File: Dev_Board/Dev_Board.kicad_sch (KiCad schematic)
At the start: 24 parts, among them J1 Conn_01x04, J2 Conn_01x04

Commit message: 02/09/2024 sch
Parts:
- added D2, D3, D4, D5, D6, D7, D8: D, Diode_SMD:Nexperia_DSN0603-2_0.6x0.3mm_P0.4mm, symbol Device:D
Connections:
- net B2: now also D2.2 (A)
- net B3: now also D3.2 (A)
- net B4: now also D4.2 (A)
- net B5: now also D5.2 (A)
- net B6: now also D6.2 (A)
- net B7: now also D7.2 (A)
- net GND: now also In_Port1.1 (Pin_1), In_Port2.1 (Pin_1), Out_Port1.1 (Pin_1), Out_Port2.1 (Pin_1), Out_Port3.1 (Pin_1), Out_Port4.1 (Pin_1), Out_Port5.1 (Pin_1), Out_Port6.1 (Pin_1), TP4.1, TP5.1
- net +24V: now reaches Out_Port1.2 (Pin_2), Out_Port4.2 (Pin_2)
- net +24V: now also In_Port1.2 (Pin_2), In_Port2.2 (Pin_2), Out_Port2.2 (Pin_2), Out_Port3.2 (Pin_2), Out_Port5.2 (Pin_2), Out_Port6.2 (Pin_2), TP4.2, TP5.2
- net 3.3V renamed +3.3V
- net A1 renamed A1 (GND)
- net A8 renamed A8M (GND)
- net B1 renamed B1 (5V)
- net B8 renamed B8 (5V)
- net B8 (5V): now also D8.2 (A)

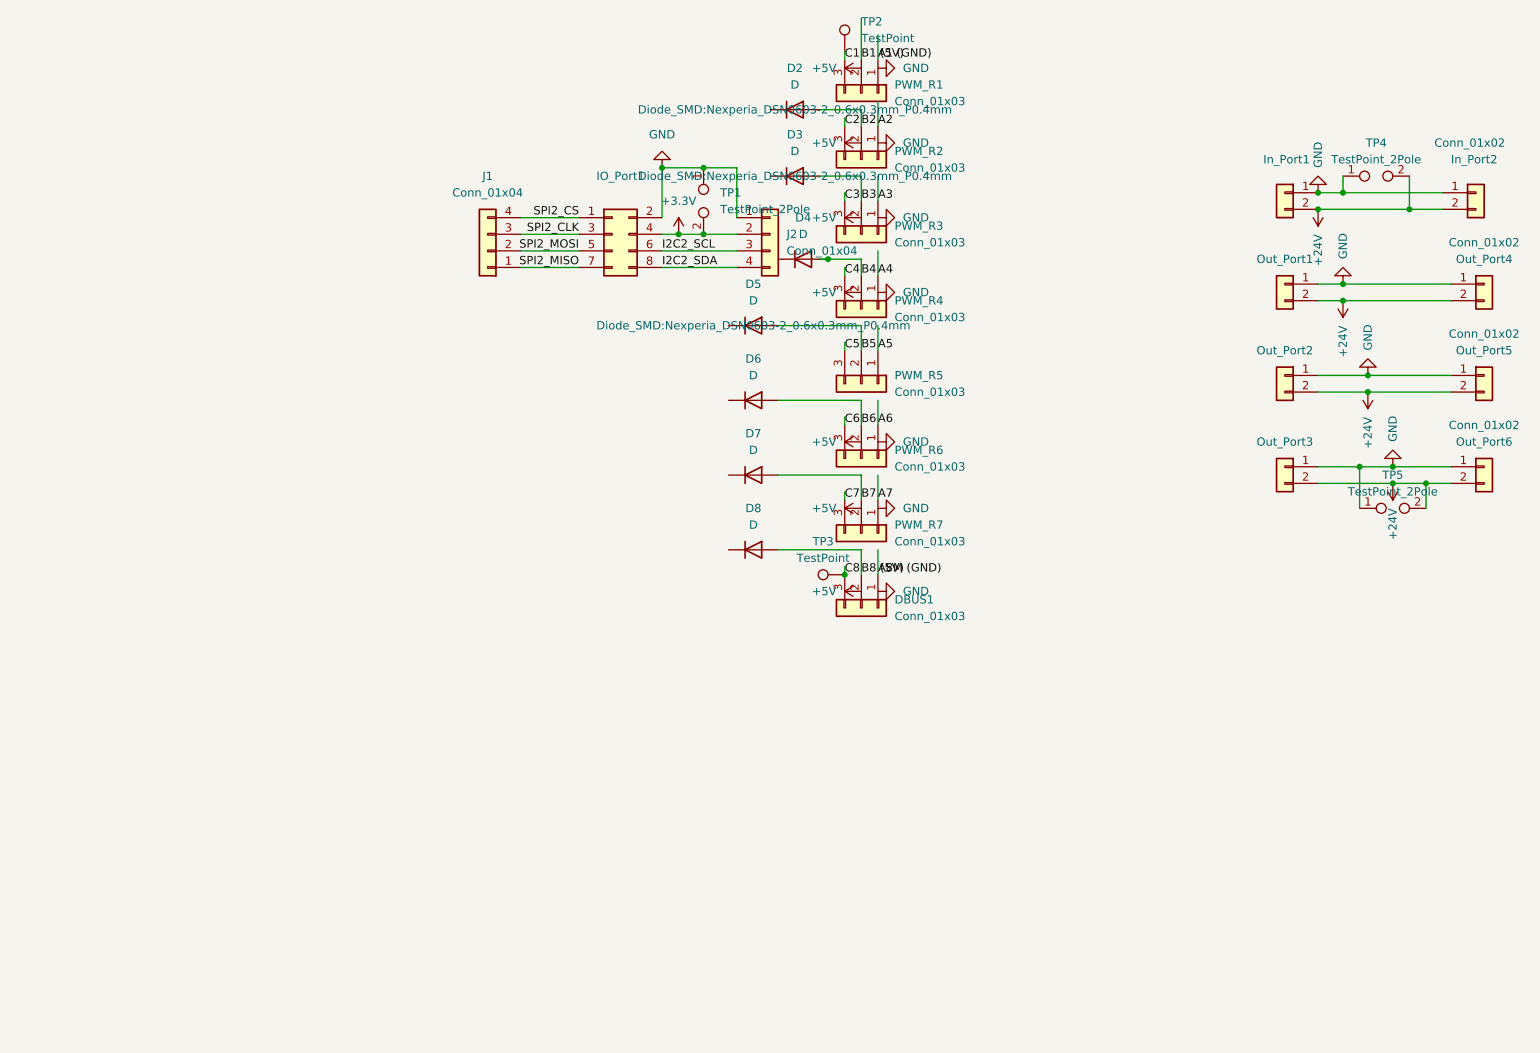
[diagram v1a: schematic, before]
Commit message: updated dimensions
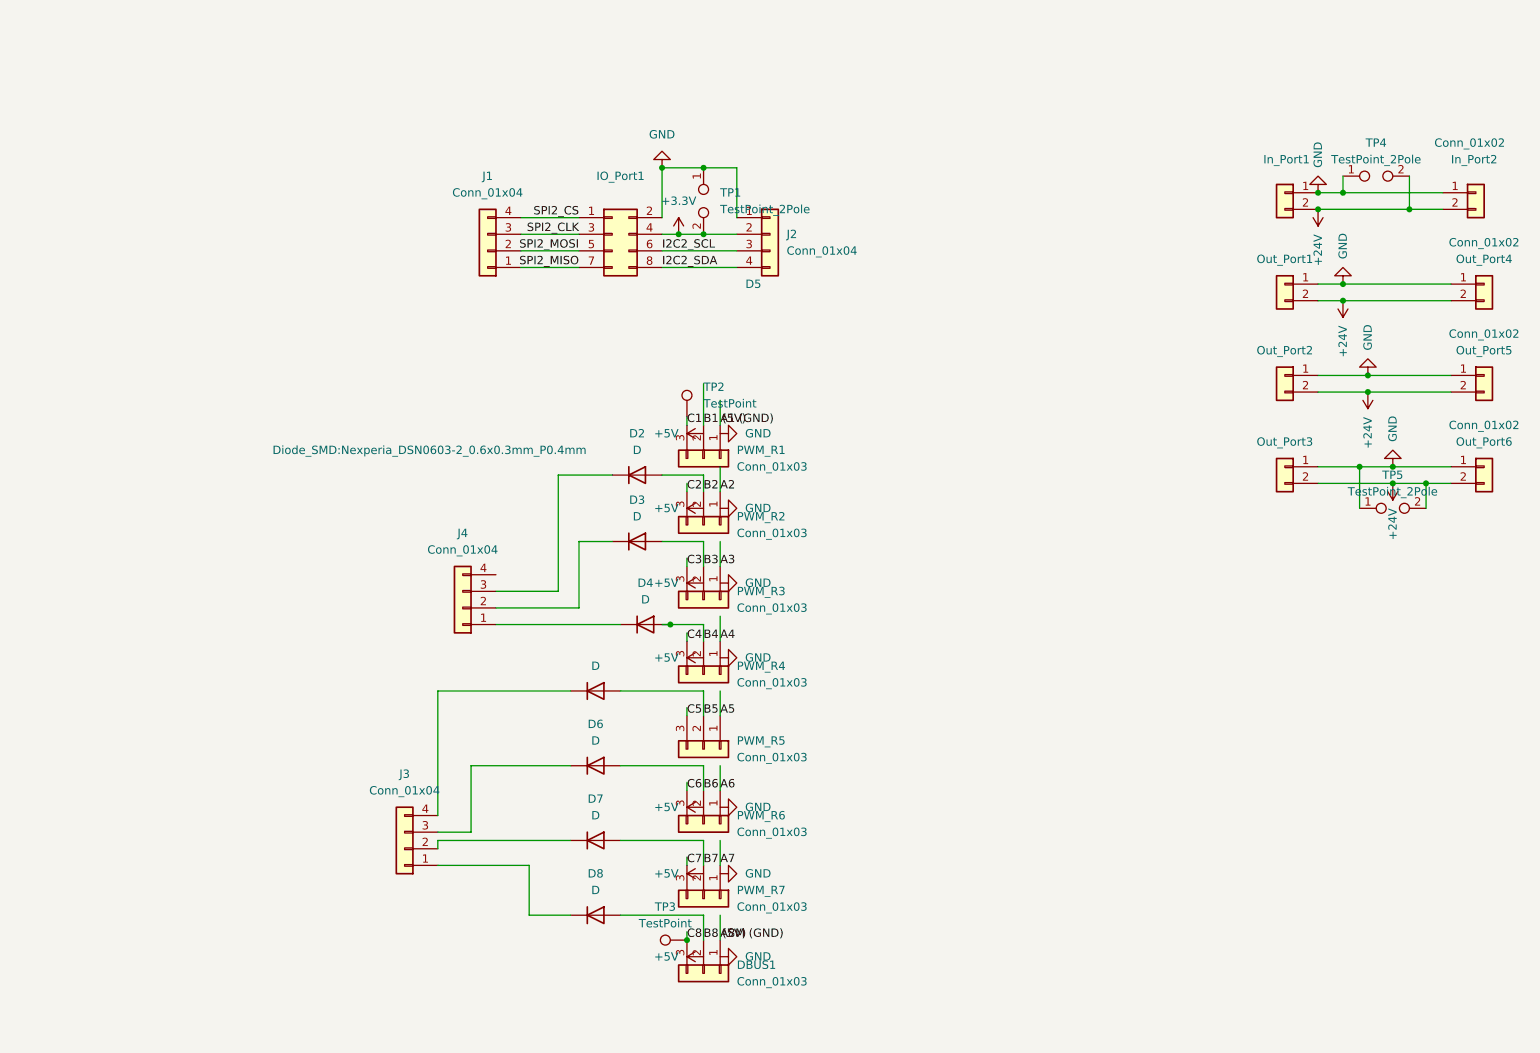
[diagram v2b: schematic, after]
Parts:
- added J3, J4: Conn_01x04, Connector_PinHeader_2.54mm:PinHeader_1x04_P2.54mm_Vertical, symbol Connector_Generic:Conn_01x04
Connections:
- net at D4.1 (K): now also J4.1 (Pin_1)
- net at D3.1 (K): now also J4.2 (Pin_2)
- net at D5.1 (K): now also J3.4 (Pin_4)
- net at D7.1 (K): now also J3.2 (Pin_2)
- net at D2.1 (K): now also J4.3 (Pin_3)
- net at D6.1 (K): now also J3.3 (Pin_3)
- net at D8.1 (K): now also J3.1 (Pin_1)
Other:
- moved on the sheet: D2, D3, D4, D5, D6, D7, D8, DBUS1, PWM_R1, PWM_R2, PWM_R3, PWM_R4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

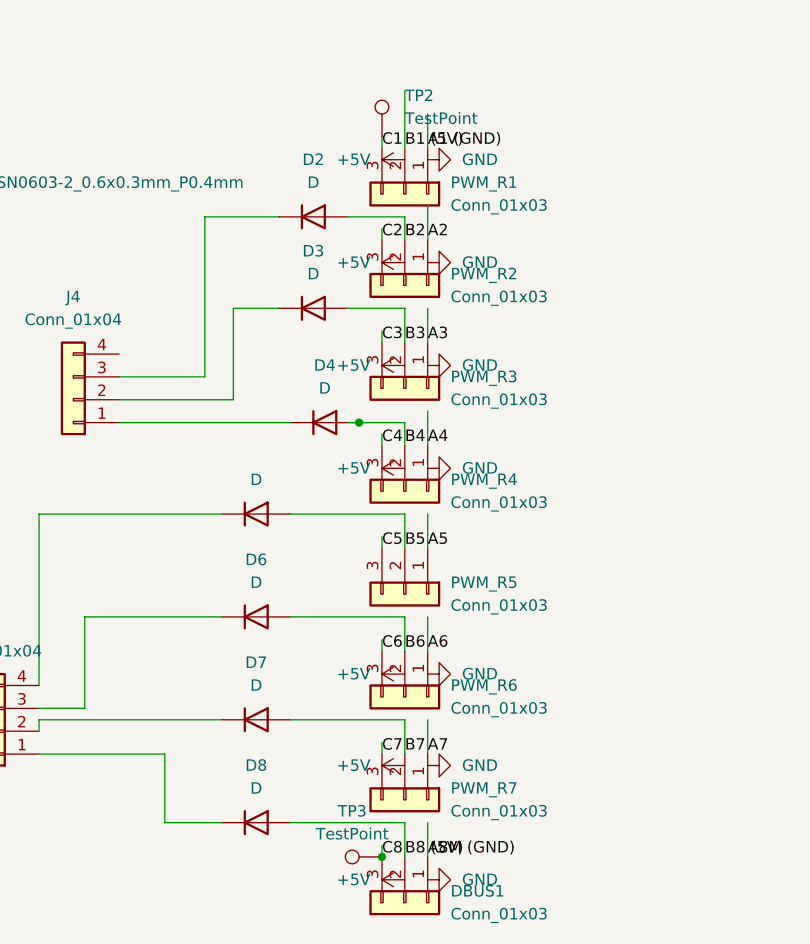
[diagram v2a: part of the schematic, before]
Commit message: Hopefully Final DevBoard. I flipped the data connectors and fixed label placement
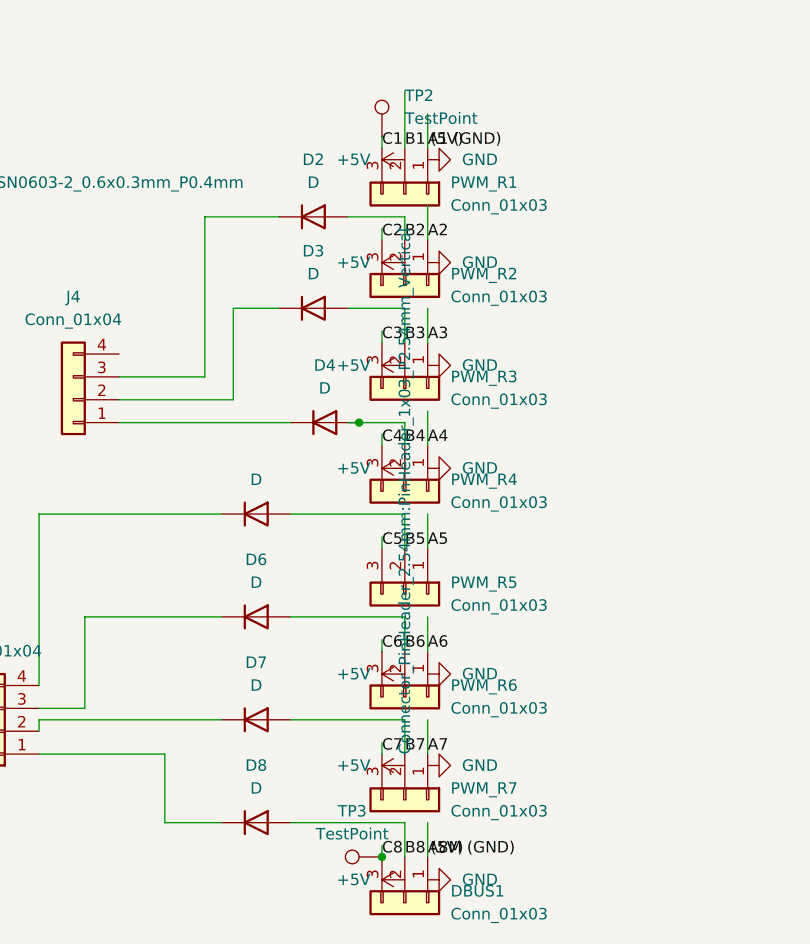
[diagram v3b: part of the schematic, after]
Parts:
- DBUS1, PWM_R1, PWM_R2, PWM_R3, PWM_R4, PWM_R5, PWM_R6, PWM_R7: footprint dev_board_footprints:PinHeader_1x03_2.54mm_Vertical_small_courtyards -> Connector_PinHeader_2.54mm:PinHeader_1x03_P2.54mm_Vertical
- In_Port1, In_Port2: footprint dev_board_footprints:AMASS_XT30UPB-M_1x02_P5.0mm_Vertical_small_courtyards -> Connector_AMASS:AMASS_XT30U-F_1x02_P5.0mm_Vertical
- Out_Port1, Out_Port2, Out_Port3, Out_Port4, Out_Port5, Out_Port6: footprint dev_board_footprints:AMASS_XT30UPB-F_1x02_P5.0mm_Vertical_small_courtyards -> Connector_AMASS:AMASS_XT30U-F_1x02_P5.0mm_Vertical
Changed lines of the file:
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@@
       (effects (font (size 1.27 1.27)) (justify left))
     )
-    (property "Footprint" "dev_board_footprints:PinHeader_1x03_2.54mm_Vertical_small_courtyards" (at 134.62 139.7 0)
+    (property "Footprint" "Connector_PinHeader_2.54mm:PinHeader_1x03_P2.54mm_Vertical" (at 134.62 139.7 0)
       (effects (font (size 1.27 1.27)) hide)
     )
@@
       (effects (font (size 1.27 1.27)))
     )
-    (property "Footprint" "dev_board_footprints:AMASS_XT30UPB-F_1x02_P5.0mm_Vertical_small_courtyards" (at 254 68.58 0)
+    (property "Footprint" "Connector_AMASS:AMASS_XT30U-F_1x02_P5.0mm_Vertical" (at 254 68.58 0)
       (effects (font (size 1.27 1.27)) hide)
     )
@@
       (effects (font (size 1.27 1.27)) (justify left))
     )
-    (property "Footprint" "dev_board_footprints:PinHeader_1x03_2.54mm_Vertical_small_courtyards" (at 134.62 162.56 0)
+    (property "Footprint" "Connector_PinHeader_2.54mm:PinHeader_1x03_P2.54mm_Vertical" (at 134.62 162.56 0)
       (effects (font (size 1.27 1.27)) hide)
     )
@@
       (effects (font (size 1.27 1.27)) (justify left))
     )
-    (property "Footprint" "dev_board_footprints:AMASS_XT30UPB-M_1x02_P5.0mm_Vertical_small_courtyards" (at 252.73 54.61 0)
+    (property "Footprint" "Connector_AMASS:AMASS_XT30U-F_1x02_P5.0mm_Vertical" (at 252.73 54.61 0)
       (effects (font (size 1.27 1.27)) hide)
     )
@@
       (effects (font (size 1.27 1.27)) hide)
     )
-    (property "Footprint" "dev_board_footprints:AMASS_XT30UPB-F_1x02_P5.0mm_Vertical_small_courtyards" (at 223.52 82.55 0)
+    (property "Footprint" "Connector_AMASS:AMASS_XT30U-F_1x02_P5.0mm_Vertical" (at 223.52 82.55 0)
       (effects (font (size 1.27 1.27)) hide)
     )
@@
       (effects (font (size 1.27 1.27)) (justify left))
     )
-    (property "Footprint" "dev_board_footprints:PinHeader_1x03_2.54mm_Vertical_small_courtyards" (at 134.62 116.84 0)
+    (property "Footprint" "Connector_PinHeader_2.54mm:PinHeader_1x03_P2.54mm_Vertical" (at 134.62 116.84 0)
       (effects (font (size 1.27 1.27)) hide)
     )
@@
       (effects (font (size 1.27 1.27)))
     )
-    (property "Footprint" "dev_board_footprints:AMASS_XT30UPB-F_1x02_P5.0mm_Vertical_small_courtyards" (at 254 96.52 0)
+    (property "Footprint" "Connector_AMASS:AMASS_XT30U-F_1x02_P5.0mm_Vertical" (at 254 96.52 0)
       (effects (font (size 1.27 1.27)) hide)
     )
@@
       (effects (font (size 1.27 1.27)) (justify left))
     )
-    (property "Footprint" "dev_board_footprints:PinHeader_1x03_2.54mm_Vertical_small_courtyards" (at 134.62 173.99 0)
+    (property "Footprint" "Connector_PinHeader_2.54mm:PinHeader_1x03_P2.54mm_Vertical" (at 134.62 173.99 0)
       (effects (font (size 1.27 1.27)) hide)
     )
@@
       (effects (font (size 1.27 1.27)) (justify left) hide)
     )
-    (property "Footprint" "dev_board_footprints:AMASS_XT30UPB-M_1x02_P5.0mm_Vertical_small_courtyards" (at 223.52 54.61 0)
+    (property "Footprint" "Connector_AMASS:AMASS_XT30U-F_1x02_P5.0mm_Vertical" (at 223.52 54.61 0)
       (effects (font (size 1.27 1.27)) hide)
     )
@@
       (effects (font (size 1.27 1.27)) hide)
     )
-    (property "Footprint" "dev_board_footprints:AMASS_XT30UPB-F_1x02_P5.0mm_Vertical_small_courtyards" (at 223.52 96.52 0)
+    (property "Footprint" "Connector_AMASS:AMASS_XT30U-F_1x02_P5.0mm_Vertical" (at 223.52 96.52 0)
       (effects (font (size 1.27 1.27)) hide)
     )
@@
       (effects (font (size 1.27 1.27)) (justify left))
     )
-    (property "Footprint" "dev_board_footprints:PinHeader_1x03_2.54mm_Vertical_small_courtyards" (at 134.62 105.41 0)
+    (property "Footprint" "Connector_PinHeader_2.54mm:PinHeader_1x03_P2.54mm_Vertical" (at 134.62 105.41 0)
       (effects (font (size 1.27 1.27)) hide)
     )
@@
   )
   (symbol (lib_id "Connector_Generic:Conn_01x02") (at 254 82.55 0) (unit 1)
-    (in_bom yes) (on_board yes) (dnp no)
+    (in_bom yes) (on_board no) (dnp no)
     (property "Reference" "Out_Port5" (at 254 78.74 0)
       (effects (font (size 1.27 1.27)))
@@
       (effects (font (size 1.27 1.27)))
     )
-    (property "Footprint" "dev_board_footprints:AMASS_XT30UPB-F_1x02_P5.0mm_Vertical_small_courtyards" (at 254 82.55 0)
+    (property "Footprint" "Connector_AMASS:AMASS_XT30U-F_1x02_P5.0mm_Vertical" (at 254 82.55 0)
       (effects (font (size 1.27 1.27)) hide)
     )
@@
       (effects (font (size 1.27 1.27)) hide)
     )
-    (property "Footprint" "dev_board_footprints:AMASS_XT30UPB-F_1x02_P5.0mm_Vertical_small_courtyards" (at 223.52 68.58 0)
+    (property "Footprint" "Connector_AMASS:AMASS_XT30U-F_1x02_P5.0mm_Vertical" (at 223.52 68.58 0)
       (effects (font (size 1.27 1.27)) hide)
     )
@@
       (effects (font (size 1.27 1.27)) (justify left))
     )
-    (property "Footprint" "dev_board_footprints:PinHeader_1x03_2.54mm_Vertical_small_courtyards" (at 134.62 95.25 0)
+    (property "Footprint" "Connector_PinHeader_2.54mm:PinHeader_1x03_P2.54mm_Vertical" (at 134.62 95.25 0)
       (effects (font (size 1.27 1.27)) hide)
     )
@@
       (effects (font (size 1.27 1.27)) (justify left))
     )
-    (property "Footprint" "dev_board_footprints:PinHeader_1x03_2.54mm_Vertical_small_courtyards" (at 134.62 128.27 0)
-      (effects (font (size 1.27 1.27)) hide)
+    (property "Footprint" "Connector_PinHeader_2.54mm:PinHeader_1x03_P2.54mm_Vertical" (at 134.62 128.27 0)
+      (effects (font (size 1.27 1.27)))
     )
     (property "Datasheet" "~" (at 134.62 128.27 0)
@@
       (effects (font (size 1.27 1.27)) (justify left))
     )
-    (property "Footprint" "dev_board_footprints:PinHeader_1x03_2.54mm_Vertical_small_courtyards" (at 134.62 151.13 0)
-      (effects (font (size 1.27 1.27)) hide)
-    )
+    (property "Footprint" "Connector_PinHeader_2.54mm:PinHeader_1x03_P2.54mm_Vertical" (at 134.62 151.13 0)
+      (effects (font (size 1.27 1.27)) hide)
+    )
